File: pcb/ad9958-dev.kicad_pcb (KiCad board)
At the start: 4 copper layers, 117 parts, among them J1 5V, J3 OUT0p, J4 OUT0n,1p, J5 15V, Q1 BFS17W, Q2 BFS17W, Q3 BFS17W, Q4 BFS17W, U1 LD1117V33, U2 LD1117V18, U3 AD9958, U4 LMV358, X1 25 MHz

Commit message: PCB almost done
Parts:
- removed C11, C46, C5: 47u, passive:C-ALUM-6.3mm
- removed C18, C26, C40, C41, C42, C44, C48, C49, C50, C53, C54: 220n, IPC7351-Nominal:CAPC2012X70
- removed C39, C43, C45, C47, C51, C52: 1n, IPC7351-Nominal:CAPC1005X55
- removed D1: 1N5822, semi:DO-201
- removed D2, D3: BAT54, IPC-semi-nominal:SOT-23
- removed E5, E6, E7, E8: 600, IPC7351-Nominal:INDC1005X60
- removed J1: 5V, conn:CONN_2-WIRES
- removed JP1: SEL0n, conn:JUMPER-SOLDER-3
- removed JP2: SEL1p, conn:JUMPER-SOLDER-3
- removed Q1, Q2, Q3, Q4: BFS17W, IPC-semi-nominal:SOT-323
- removed R34, R35: 49r9, IPC7351-Nominal:RESC1005X40
- added J2: 5V, conn:CONN_3-SIL, F.Cu at (175.3, 97.8)
- C1, C13, C14, C15, C16, C17, C19, C2, C20, C21, C22, C23, C28, C3, C6, C7, C8, E1, E2, E3, E4: moved to B.Cu
- C29: value 1n -> 100n; moved to B.Cu
- C30, C36: value 1n -> 10n; moved to B.Cu
- C31, C35: value 220n -> 10n; footprint IPC7351-Nominal:CAPC2012X70 -> IPC7351-Nominal:CAPC1005X55; moved to B.Cu
- C32, C33, C37: value 220n -> 10u; moved to B.Cu
- C34: value 220n -> 100n; footprint IPC7351-Nominal:CAPC2012X70 -> IPC7351-Nominal:CAPC1005X55; moved to B.Cu
- C38: value 1n -> 10u; footprint IPC7351-Nominal:CAPC1005X55 -> IPC7351-Nominal:CAPC2012X70; moved to B.Cu
- J3: value OUT0p -> OUT0
- J4: value OUT0n,1p -> OUT1
- J5: value 15V -> HEAD-M10X2; footprint conn:CONN_2-WIRES -> conn:CONN_20-DIL
- R13, R16: value 75 -> 49r9
- R15, R17: value 220 -> 49r9; footprint IPC7351-Nominal:RESC1608X50 -> IPC7351-Nominal:RESC1005X40
- R18: value 360 -> 53r6
- R19: value 75 -> 53r6
- R20: value 3k3 -> 360
- R21: value 75 -> 360
- R22: value NP -> 360
- R23, R29, R30: value 10k -> 360
- R24: value 49r9 -> 2k2
- R25: value 10k -> 53r6
- R26: value 49r9 -> 53r6
- R27, R28: value 100 -> 360
- R31: value 360 -> 2k2
- R32: value 3k3 -> 49r9
- R33: value NP -> 49r9
- U1: value LD1117V33 -> LM1117-FIXED-SOT223; footprint semi:TO-220 -> IPC-semi-nominal:SOT-223
- U2: value LD1117V18 -> LMH6714; footprint semi:TO-220 -> IPC-semi-nominal:SOT-23-5
- U4: value LMV358 -> LMH6714; footprint IPC7351-Nominal:SOP65P490X110-8B -> IPC-semi-nominal:SOT-23-5
- moved C1 124.3 mm to (149.0, 85.8)
- moved R4 121.6 mm to (151.0, 90.5), turned to 270 degrees
- moved C2 119.5 mm to (149.0, 83.8)
- moved E1 119.4 mm to (150.5, 78.0), turned to 90 degrees
- moved C8 117.2 mm to (155.8, 80.0), turned to 270 degrees
- moved C14 117.1 mm to (151.0, 88.0), turned to 90 degrees
- moved R11 116.0 mm to (155.0, 77.5), turned to 270 degrees
- moved C3 115.7 mm to (149.0, 82.2)
- moved C9 115.1 mm to (149.0, 69.5)
- moved R2 113.4 mm to (159.0, 90.5), turned to 270 degrees
- moved R12 111.5 mm to (149.0, 77.5), turned to 90 degrees
- moved C15 110.0 mm to (157.0, 84.8), turned to 180 degrees
- moved C6 109.3 mm to (150.5, 80.0), turned to 270 degrees
- moved R6 109.2 mm to (153.0, 90.5), turned to 270 degrees
- moved C27 107.2 mm to (150.0, 77.5), turned to 90 degrees
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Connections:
- C29 pad 1: Net-(C29-Pad1) -> +5
- C29 pad 2: GND -> -5
- C30 pad 1: Net-(C30-Pad1) -> +5
- C31 pad 1: Net-(C29-Pad1) -> GND
- C31 pad 2: GND -> -5
- C32 pad 1: Net-(C30-Pad1) -> +5
- C33 pad 1: Net-(C33-Pad1) -> GND
- C33 pad 2: GND -> -5
- C34 pad 1: Net-(C34-Pad1) -> +5
- C34 pad 2: GND -> -5
- C35 pad 1: Net-(C35-Pad1) -> +5
- C35 pad 2: Net-(C35-Pad2) -> GND
- C36 pad 1: Net-(C35-Pad1) -> GND
- C36 pad 2: Net-(C35-Pad2) -> -5
- C37 pad 1: Net-(C37-Pad1) -> +5
- C37 pad 2: Net-(C37-Pad2) -> GND
- C38 pad 1: Net-(C37-Pad1) -> GND
- C38 pad 2: Net-(C37-Pad2) -> -5
- C4 pad 1: Net-(C4-Pad1) -> +3.3
- E2 pad 1: Net-(D2-Pad3) -> +5
- E3 pad 1: Net-(E3-Pad1) -> -5
- E4 pad 1: Net-(C29-Pad1) -> +3.3
- E4 pad 2: +15 -> Net-(E4-Pad2)
- J3 pad 1: Net-(C42-Pad1) -> Net-(J3-Pad1)
- J4 pad 1: Net-(C44-Pad1) -> Net-(J4-Pad1)
- J5 pad 1: Net-(E8-Pad2) -> GND
- J5 pad 2: GND -> Net-(J5-Pad2)
- R1 pad 2: Net-(J2-Pad4) -> Net-(J5-Pad2)
- R13 pad 2: Net-(R13-Pad2) -> /C0P
- R15 pad 1: Net-(C29-Pad1) -> /+1v8A
- R15 pad 2: Net-(C35-Pad2) -> /C0N
- R16 pad 1: Net-(JP1-Pad1) -> /+1v8A
- R16 pad 2: +1.8 -> /C1P
- R17 pad 1: Net-(C30-Pad1) -> /+1v8A
- R17 pad 2: Net-(C37-Pad2) -> /C1N
- R18 pad 1: Net-(E3-Pad1) -> /+1v8A
- R18 pad 2: GND -> /C1P
- R19 pad 1: Net-(E2-Pad2) -> /+1v8A
- R19 pad 2: Net-(JP1-Pad1) -> /C1N
- R2 pad 2: Net-(J2-Pad6) -> Net-(J5-Pad16)
- R20 pad 1: Net-(C40-Pad1) -> Net-(R20-Pad1)
- R20 pad 2: Net-(C37-Pad1) -> /C1P
- R21 pad 1: Net-(E3-Pad1) -> Net-(R21-Pad1)
- R21 pad 2: Net-(R13-Pad2) -> /C1N
- R22 pad 1: Net-(C37-Pad1) -> Net-(R22-Pad1)
- R22 pad 2: GND -> Net-(R20-Pad1)
- R23 pad 1: Net-(C33-Pad1) -> GND
- R23 pad 2: /+1v8A -> Net-(R21-Pad1)
- R24 pad 1: Net-(Q4-Pad2) -> Net-(R22-Pad1)
- R24 pad 2: GND -> -5
- R25 pad 1: Net-(C34-Pad1) -> /+1v8A
- R25 pad 2: /+1v8A -> /C0P
- R26 pad 1: Net-(C44-Pad2) -> /+1v8A
- R26 pad 2: Net-(Q4-Pad2) -> /C0N
- R27 pad 1: Net-(C51-Pad2) -> Net-(R27-Pad1)
- R27 pad 2: Net-(C49-Pad1) -> /C0P
- R28 pad 1: Net-(C52-Pad2) -> Net-(R28-Pad1)
- R28 pad 2: Net-(C50-Pad1) -> /C0N
- R29 pad 1: Net-(E2-Pad2) -> Net-(R29-Pad1)
- R29 pad 2: Net-(C49-Pad2) -> Net-(R27-Pad1)
- R3 pad 2: Net-(J2-Pad8) -> Net-(J5-Pad18)
- R30 pad 1: Net-(E3-Pad1) -> GND
- R30 pad 2: Net-(C50-Pad2) -> Net-(R28-Pad1)
- R31 pad 1: Net-(E2-Pad2) -> Net-(R29-Pad1)
- R31 pad 2: GND -> -5
- R32 pad 1: Net-(C39-Pad1) -> Net-(J3-Pad1)
- R32 pad 2: Net-(C35-Pad1) -> Net-(R22-Pad1)
- R33 pad 1: Net-(C35-Pad1) -> Net-(J4-Pad1)
- R33 pad 2: GND -> Net-(R29-Pad1)
- R4 pad 2: Net-(J2-Pad10) -> Net-(J5-Pad4)
- R5 pad 2: Net-(J2-Pad12) -> Net-(J5-Pad6)
- R6 pad 2: Net-(J2-Pad14) -> Net-(J5-Pad8)
- R7 pad 2: Net-(J2-Pad16) -> Net-(J5-Pad10)
- R8 pad 2: Net-(J2-Pad18) -> Net-(J5-Pad12)
- R9 pad 2: Net-(J2-Pad20) -> Net-(J5-Pad14)
- U1 pad 2: +3.3 -> +1.8
- U1 pad 3: Net-(C4-Pad1) -> +3.3
- U2 pad 1: GND -> Net-(R22-Pad1)
- U2 pad 2: +1.8 -> -5
- U2 pad 3: Net-(C4-Pad1) -> Net-(R21-Pad1)
- U3 pad 13: /+1v8A -> /C1P
- U3 pad 14: Net-(R13-Pad2) -> /C1N
- U3 pad 8: Net-(JP1-Pad2) -> /C0P
- U3 pad 9: Net-(JP2-Pad2) -> /C0N
- U4 pad 1: Net-(C50-Pad1) -> Net-(R29-Pad1)
- U4 pad 2: Net-(C50-Pad2) -> -5
- U4 pad 3: Net-(C34-Pad1) -> Net-(R28-Pad1)
- U4 pad 4: GND -> Net-(R27-Pad1)
- U4 pad 5: Net-(C33-Pad1) -> +5
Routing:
- net GND: track 0.00 -> 260.6 mm, vias 0 -> 30
- net /+1v8A: track 0.00 -> 27.4 mm, vias 0 -> 16
- net Net-(C10-Pad1): track 0.00 -> 15.2 mm
- net +3.3: track 0.00 -> 14.4 mm, vias 0 -> 1
- net /C0P: track 0.00 -> 13.7 mm, vias 0 -> 2
- net +1.8: track 0.00 -> 13.6 mm, vias 0 -> 2
- net /C0N: track 0.00 -> 13.3 mm, vias 0 -> 2
- net Net-(C9-Pad1): track 0.00 -> 12.1 mm
- net /C1N: track 0.00 -> 9.82 mm, vias 0 -> 3
- net /C1P: track 0.00 -> 9.32 mm, vias 0 -> 3
- net /PWR_DWN_CTL: track 0.00 -> 6.27 mm
- net Net-(R20-Pad1): track 0.00 -> 5.53 mm
- net Net-(R27-Pad1): track 0.00 -> 5.50 mm
- net /MASTER_RESET: track 0.00 -> 5.18 mm
- net Net-(J4-Pad1): track 0.00 -> 4.80 mm
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- added copper zone on In2.Cu, net /+1v8A
- added copper zone on B.Cu, net GND
- added copper zone on In1.Cu, net GND
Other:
- board outline added: 40 x 32 mm
- board text added: "Z0=50"

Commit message: PCB almost done
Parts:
- moved C24 1.27 mm to (164.8, 80.2), turned to 45 degrees
- moved C25 0.35 mm to (164.8, 86.5)
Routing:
- net GND: track 260.6 -> 318.6 mm, vias 30 -> 41
- net +3.3: track 14.4 -> 62.0 mm
- net +1.8: track 13.6 -> 55.9 mm, vias 2 -> 8
- net /+1v8A: track 27.4 -> 64.1 mm, vias 16 -> 23
- net +5: track 0.00 -> 24.7 mm, vias 0 -> 3
- net -5: track 2.98 -> 25.3 mm, vias 0 -> 2
- net Net-(E4-Pad2): track 0.00 -> 20.5 mm
- net Net-(J5-Pad18): track 0.00 -> 10.6 mm
- net Net-(J5-Pad14): track 0.00 -> 8.89 mm
- net Net-(J5-Pad12): track 0.00 -> 8.37 mm
- net Net-(J5-Pad16): track 0.00 -> 8.13 mm
- net Net-(J5-Pad10): track 0.00 -> 6.80 mm
- net Net-(J5-Pad2): track 0.00 -> 6.35 mm
- net Net-(R14-Pad1): track 1.53 -> 7.62 mm
- net Net-(J5-Pad8): track 0.00 -> 5.57 mm
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- added copper zone on In2.Cu, net +1.8

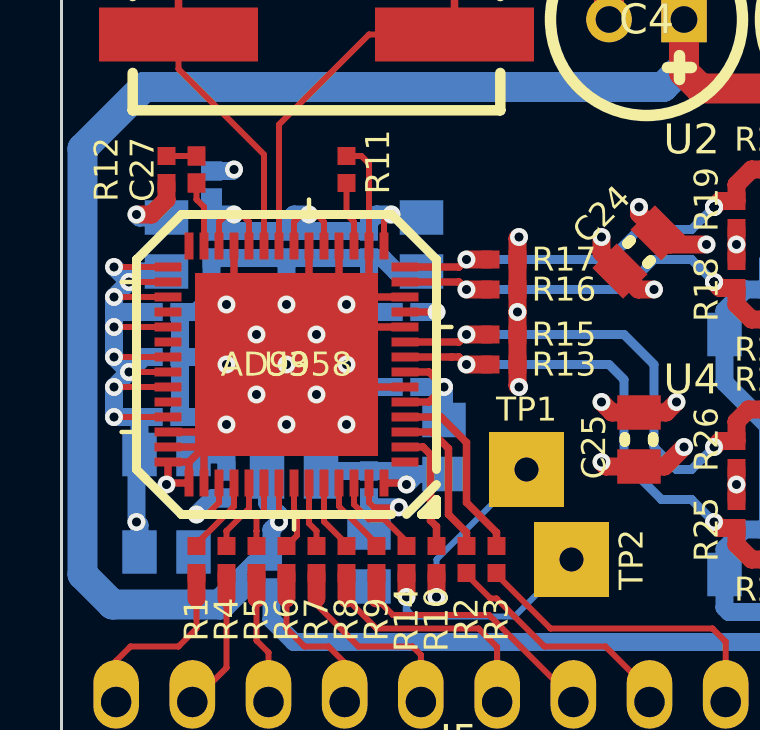
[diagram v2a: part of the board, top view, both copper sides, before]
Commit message: Updated AD9958 footprint.
Still have to re-route a couple signals
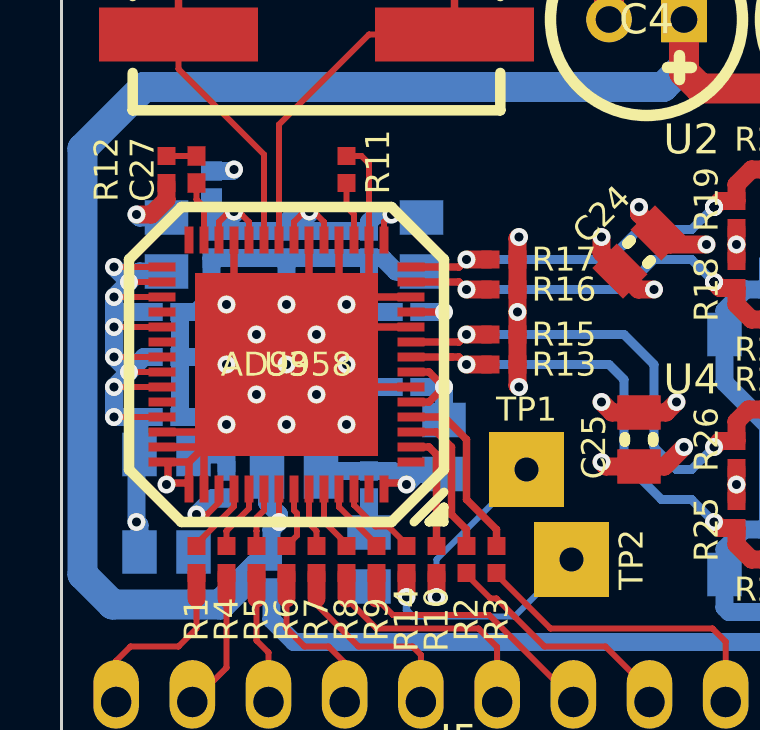
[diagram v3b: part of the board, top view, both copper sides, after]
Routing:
- net +1.8: track 55.9 -> 53.3 mm, vias 8 -> 7
- net /+1v8A: track 64.1 -> 63.2 mm
- net GND: track 318.6 -> 319.4 mm

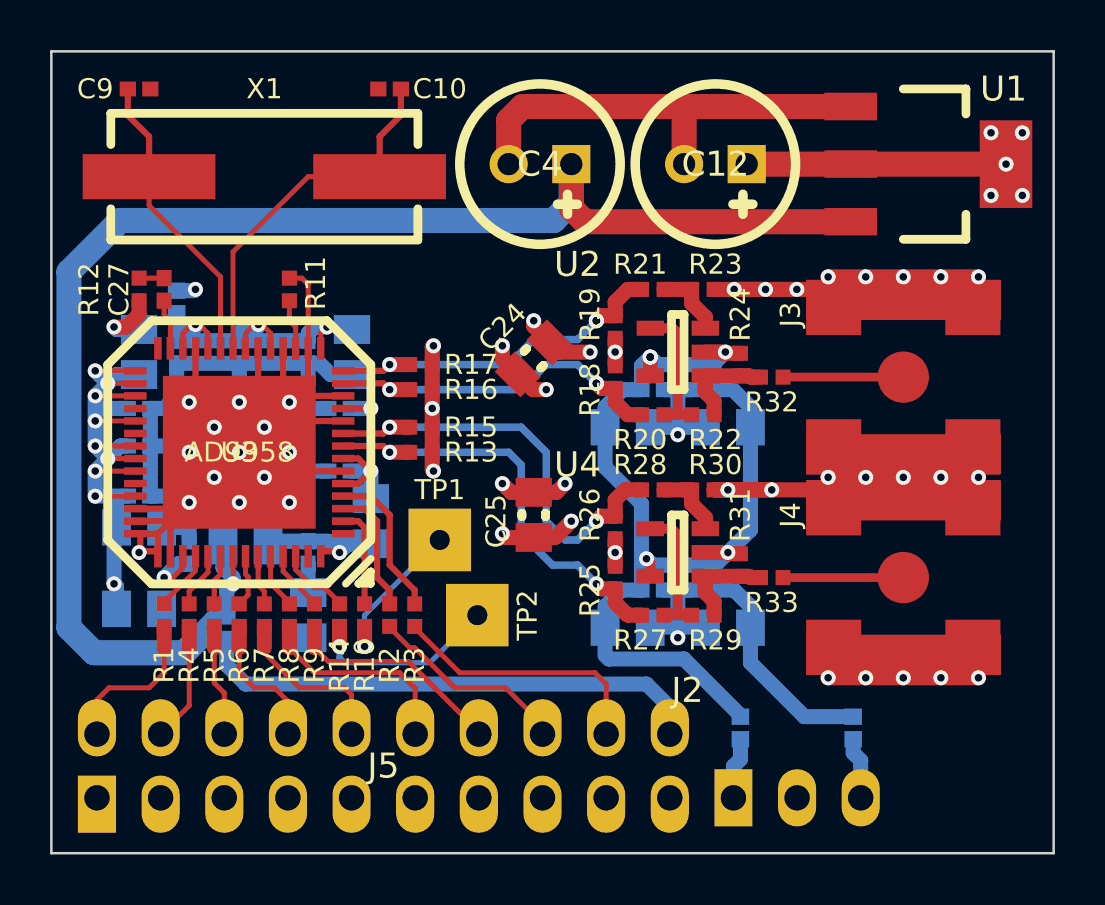
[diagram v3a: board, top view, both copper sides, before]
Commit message: Added power protection, touched up PCB
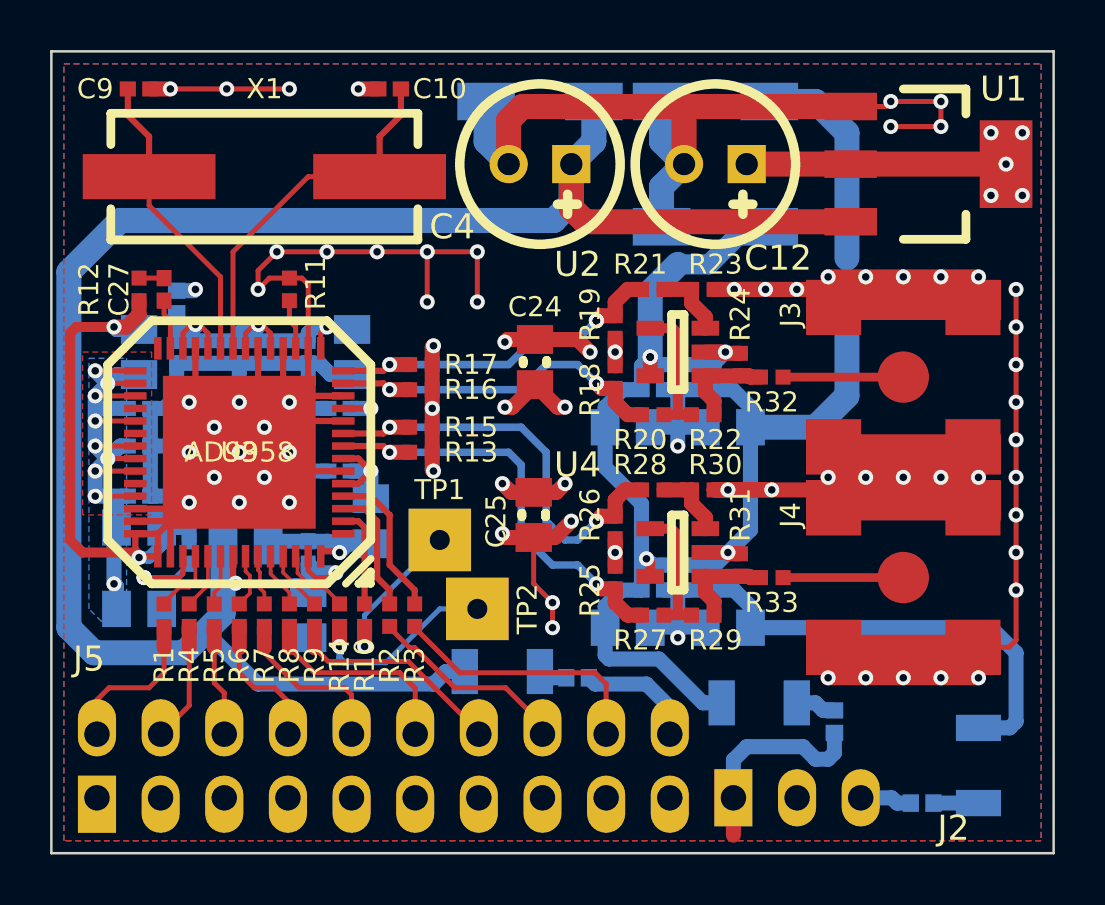
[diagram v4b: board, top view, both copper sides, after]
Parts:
- added D1: SS12, IPC7351-Nominal:DIOM5326X292, B.Cu at (165.0, 70.0)
- added D2: SS12, IPC7351-Nominal:DIOM5326X292, B.Cu at (172.0, 75.0)
- added D3: SS12, IPC7351-Nominal:DIOM5326X292, B.Cu at (172.0, 70.0)
- added R34: 250mA, IPC7351-Nominal:RESC3216X60, B.Cu at (163.5, 92.8)
- added R35: 100mA, IPC7351-Nominal:RESC3216X60, B.Cu at (173.8, 94.0)
- added R36: 100mA, IPC7351-Nominal:RESC3216X60, B.Cu at (182.5, 96.5)
- moved E4 14.1 mm to (166.5, 93.0), turned to 0 degrees
- moved E3 4.07 mm to (180.2, 98.0), turned to 180 degrees
- moved E2 3.76 mm to (176.8, 94.8)
- moved TP2 0.25 mm to (162.5, 90.2)
- moved C24 0.16 mm to (164.8, 80.4), turned to 90 degrees
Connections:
- E2 pad 1: +5 -> Net-(E2-Pad1)
- E3 pad 1: -5 -> Net-(E3-Pad1)
- E4 pad 1: +3.3 -> Net-(E4-Pad1)
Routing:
- net GND: track 319.4 -> 394.5 mm, vias 41 -> 69
- net -5: track 25.3 -> 52.8 mm
- net Net-(E4-Pad2): track 20.5 -> 4.79 mm
- net +3.3: track 62.0 -> 75.7 mm
- net +5: track 24.7 -> 32.1 mm
- net Net-(E2-Pad2): track 2.46 -> 8.36 mm
- net +1.8: track 53.3 -> 56.8 mm, vias 7 -> 9
- net Net-(E3-Pad1): track 0.00 -> 1.80 mm
- net (no net): track 3.04 -> 1.25 mm, vias 1 -> 0
- net Net-(E2-Pad1): track 0.00 -> 1.62 mm
- net Net-(E4-Pad1): track 0.00 -> 1.15 mm
- added copper zone on B.Cu, net /+1v8A
- added copper zone on F.Cu, net /+1v8A
- added copper zone on F.Cu, net GND
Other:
- board text added: "WCP52 GAIN/PHASE SYNTHESIZER PROTO OCT 2014"

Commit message: PCB touchups
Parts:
- J2: moved to B.Cu

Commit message: Schematic touchups
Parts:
- C30, C31, C35, C36: value 10n -> 1n
- J2: moved to F.Cu
- J5: value HEAD-M10X2 -> INTERFACE
- U1: value LM1117-FIXED-SOT223 -> LM1117-1v8-SOT223
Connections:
- net /+1v8A renamed +1.8A
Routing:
- net GND: track 394.5 -> 398.1 mm, vias 69 -> 70
- net +1.8: track 56.8 -> 58.7 mm, vias 9 -> 8
- net +3.3: track 75.7 -> 77.4 mm
- net +1.8A: track 63.5 -> 64.6 mm

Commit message: PCB fixes
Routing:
- net Net-(E2-Pad2): track 8.36 -> 6.87 mm

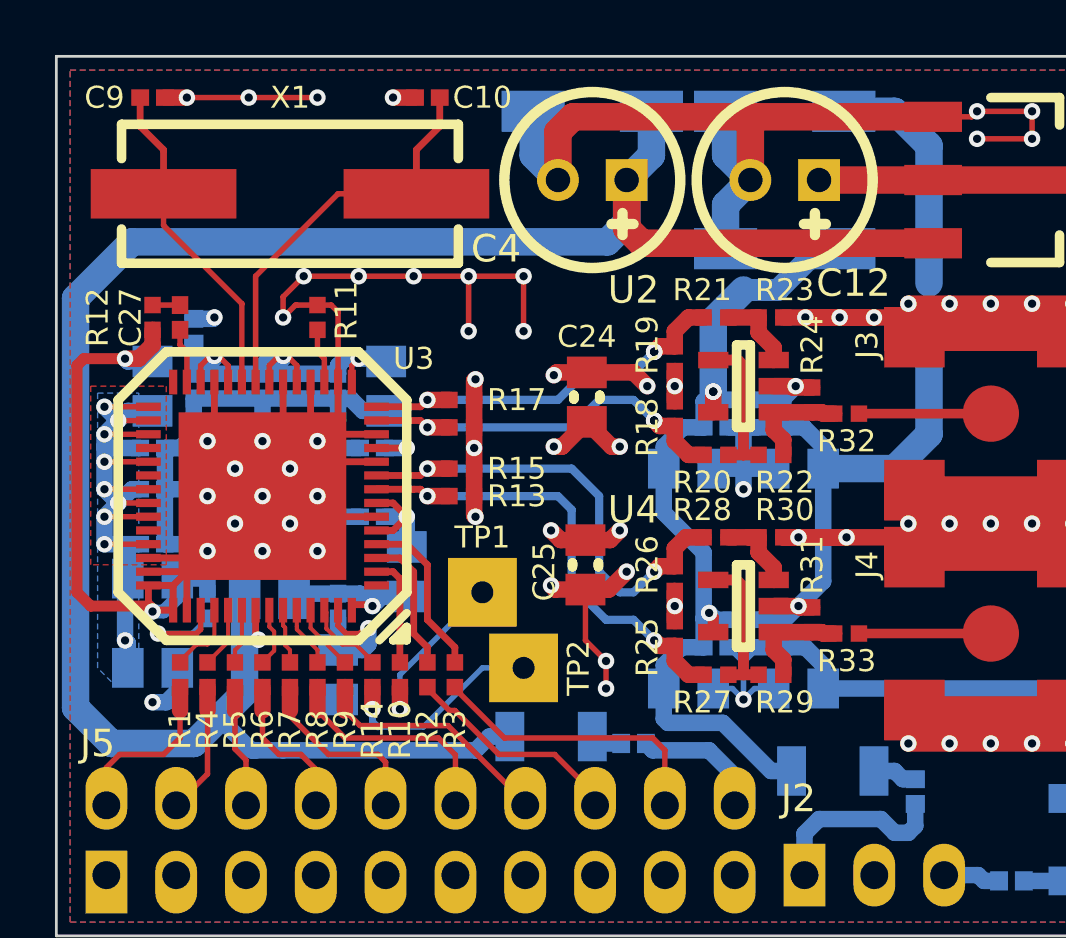
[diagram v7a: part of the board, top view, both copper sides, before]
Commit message: Reannotated components
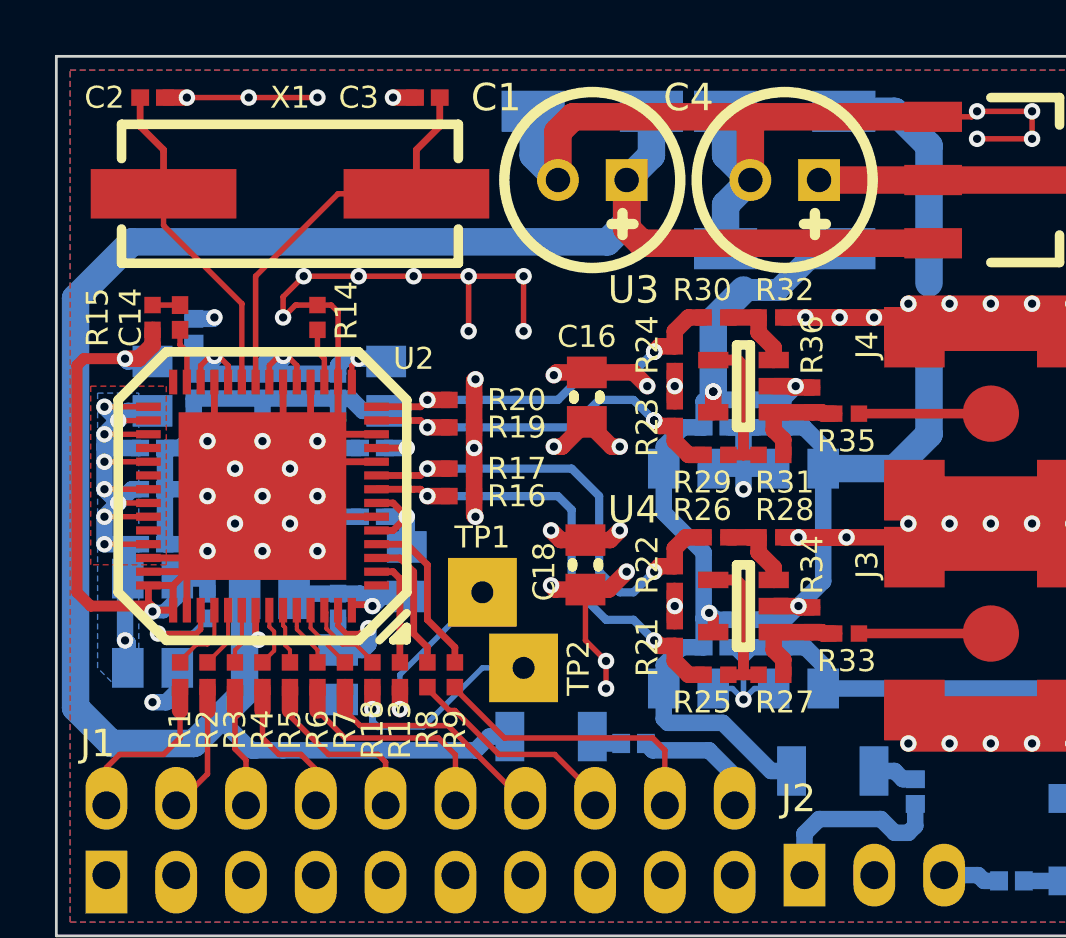
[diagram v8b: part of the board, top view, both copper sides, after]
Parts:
- renumbered C4 to C1, C21 to C10, C6 to C11, C23 to C12, C7 to C13, C27 to C14, C8 to C15, C24 to C16, C13 to C17, C25 to C18, C15 to C19, C9 to C2, C28 to C20, C14 to C21, C16 to C23, C20 to C24, C29 to C25, C30 to C26, C31 to C27, C32 to C28, C33 to C29, C10 to C3, C34 to C30, C35 to C31, C36 to C32, C37 to C33, C38 to C34, C12 to C4, C1 to C5, C17 to C6, C2 to C7, C19 to C8, C3 to C9, E4 to E1, E1 to E4, J5 to J1, J4 to J3, J3 to J4, R34 to R10, R35 to R11, R36 to R12, R10 to R13, R11 to R14, R12 to R15, R13 to R16, R15 to R17, R14 to R18, R16 to R19, R4 to R2, R17 to R20, R25 to R21, R26 to R22, R18 to R23, R19 to R24, R27 to R25, R28 to R26, R29 to R27, R30 to R28, R20 to R29, R5 to R3, R21 to R30, R22 to R31, R23 to R32, R31 to R34, R32 to R35, R24 to R36, R6 to R4, R7 to R5, R8 to R6, R9 to R7, R2 to R8, R3 to R9, U3 to U2, U2 to U3
